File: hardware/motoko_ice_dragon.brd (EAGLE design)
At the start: 91 x 88 mm, 112 parts, among them IC2 LM2937, Q1 8MHz, Q10 20mA/30V, Q11 20mA/30V, Q2 BSS138TOP, Q3 BSS138TOP, Q4 20mA/30V, Q5 20mA/30V, Q6 20mA/30V, Q7 20mA/30V, Q8 20mA/30V, Q9 20mA/30V, U1 MP6540HA, U2 STM32_STM32F722XX, U3 MP6540HA

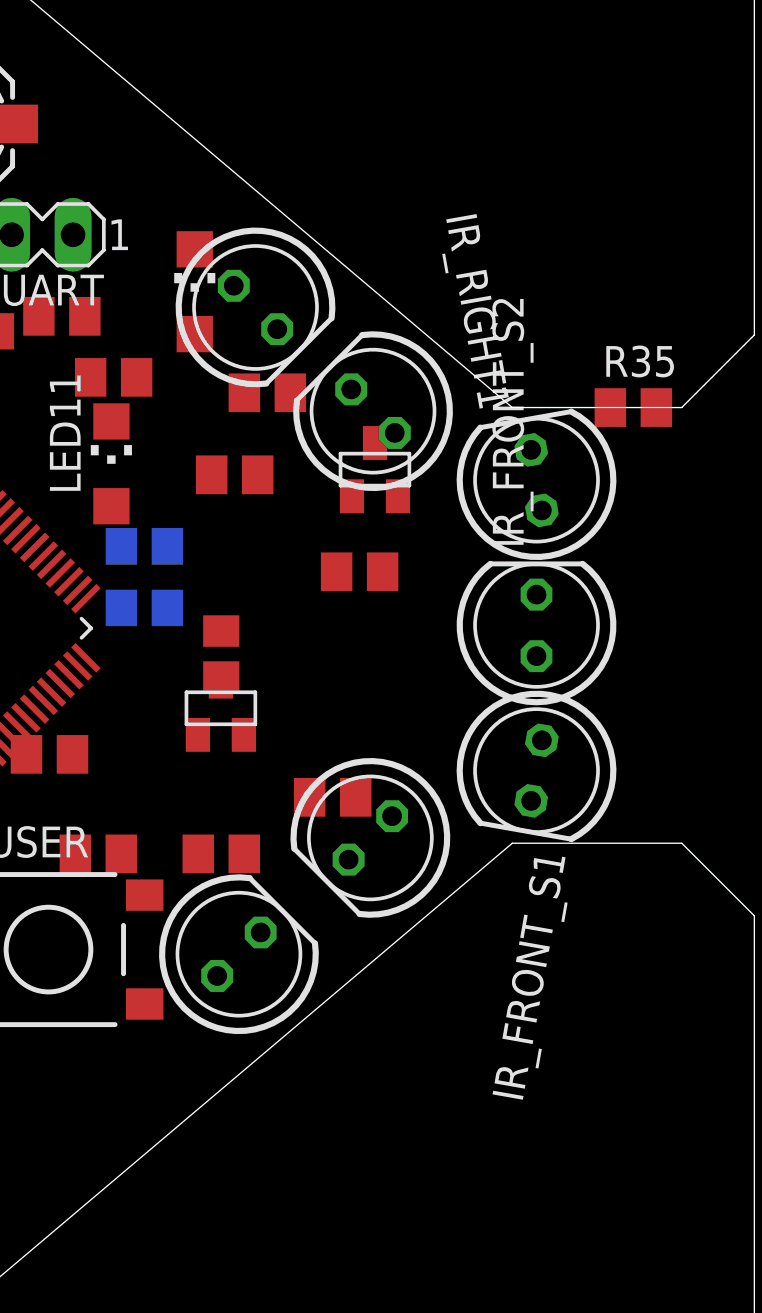
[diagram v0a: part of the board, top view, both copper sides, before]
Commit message: lqr design
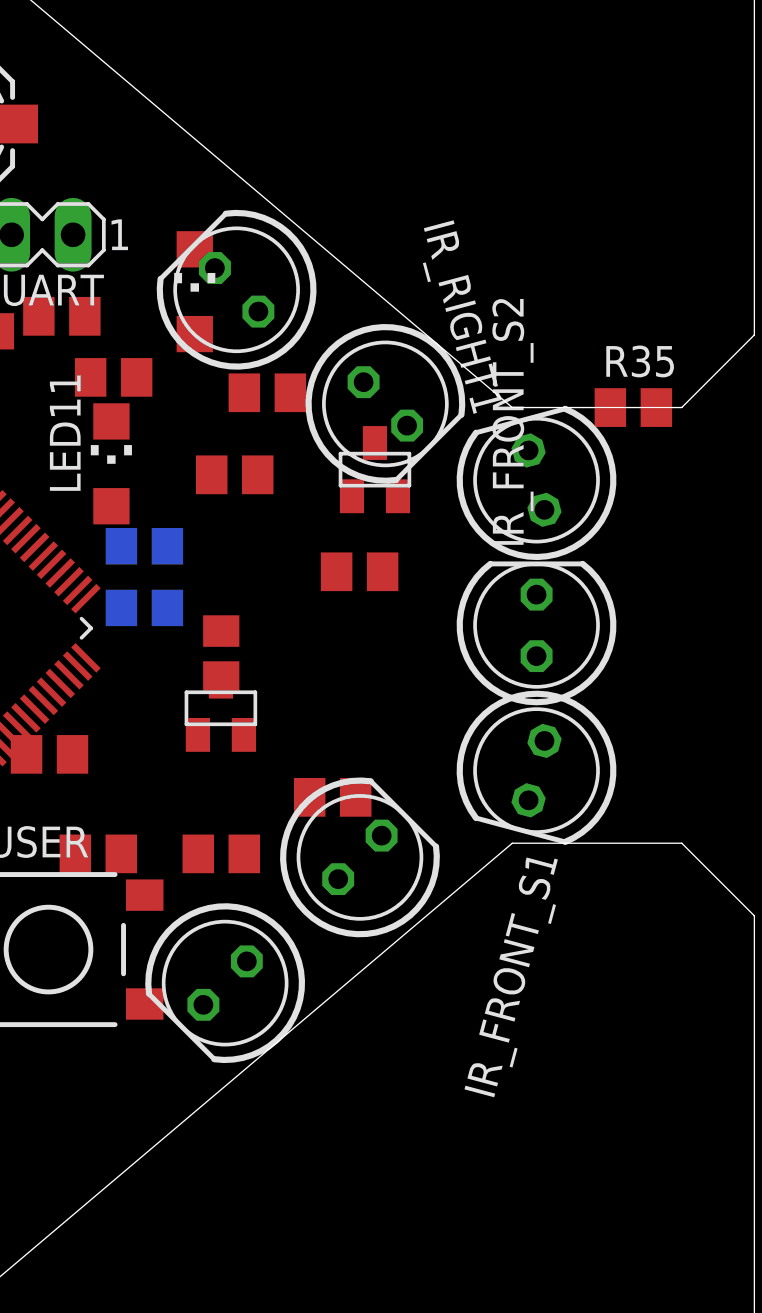
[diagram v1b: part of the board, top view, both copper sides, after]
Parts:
- moved IR_RIGHT 8.49 mm to (54.1, 30.2)
- moved IR_RIGHT_S 6.40 mm to (59.7, 35.4)
- moved IR_LEFT 1.07 mm to (54.6, 58.9), turned to 135 degrees
- moved IR_LEFT_S 0.59 mm to (60.8, 54.1), turned to 315 degrees
- turned IR_FRONT_S1 to 255 degrees
- turned IR_RIGHT1 to 105 degrees
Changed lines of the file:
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@@
 <attribute name="POPULARITY" value="0" x="47.0176" y="-14.2464" size="1.778" layer="28" rot="MR270" display="off"/>
 </element>
-<element name="IR_LEFT" library="my_parts" package="LED5MM" value="" x="55.39" y="58.135" smashed="yes" rot="R315">
-<attribute name="VALUE" x="56.377828125" y="54.59678125" size="1.27" layer="27" ratio="10" rot="R315"/>
-</element>
-<element name="IR_RIGHT" library="my_parts" package="LED5MM" value="" x="60.135" y="36.22" smashed="yes" rot="R225">
-<attribute name="VALUE" x="56.59678125" y="35.232171875" size="1.27" layer="27" ratio="10" rot="R225"/>
-</element>
-<element name="IR_LEFT_S" library="my_parts" package="LED5MM" value="" x="60.245" y="53.85" smashed="yes" rot="R135">
-<attribute name="VALUE" x="59.257171875" y="57.38821875" size="1.27" layer="27" ratio="10" rot="R135"/>
-</element>
-<element name="IR_RIGHT_S" library="my_parts" package="LED5MM" value="" x="54.705" y="31.415" smashed="yes" rot="R45">
-<attribute name="VALUE" x="58.24321875" y="32.402828125" size="1.27" layer="27" ratio="10" rot="R45"/>
+<element name="IR_LEFT" library="my_parts" package="LED5MM" value="" x="54.61" y="58.865" smashed="yes" rot="R135">
+<attribute name="VALUE" x="53.622171875" y="62.40321875" size="1.27" layer="27" ratio="10" rot="R135"/>
+</element>
+<element name="IR_RIGHT" library="my_parts" package="LED5MM" value="" x="54.135" y="30.22" smashed="yes" rot="R225">
+<attribute name="VALUE" x="50.59678125" y="29.232171875" size="1.27" layer="27" ratio="10" rot="R225"/>
+</element>
+<element name="IR_LEFT_S" library="my_parts" package="LED5MM" value="" x="60.755" y="54.15" smashed="yes" rot="R315">
+<attribute name="VALUE" x="61.742828125" y="50.61178125" size="1.27" layer="27" ratio="10" rot="R315"/>
+</element>
+<element name="IR_RIGHT_S" library="my_parts" package="LED5MM" value="" x="59.705" y="35.415" smashed="yes" rot="R45">
+<attribute name="VALUE" x="63.24321875" y="36.402828125" size="1.27" layer="27" ratio="10" rot="R45"/>
 </element>
 <element name="JP1" library="jumper" library_urn="urn:adsk.eagle:library:252" package="JP1" package3d_urn="urn:adsk.eagle:package:15455/1" value="2 CellLi-Pol" x="35.6108" y="67.6148" smashed="yes">
@@
 <element name="U$1" library="my_library" package="BRUSHLESS_GIMBAL_MOTOR_WHEEL" value="BRUSHLESS_GIMBAL_MOTOR_WHEEL" x="15" y="76" smashed="yes" rot="R270"/>
 <element name="U$2" library="my_library" package="BRUSHLESS_GIMBAL_MOTOR_WHEEL" value="BRUSHLESS_GIMBAL_MOTOR_WHEEL" x="15" y="14" smashed="yes" rot="R90"/>
-<element name="IR_FRONT_S1" library="my_parts" package="LED5MM" value="" x="67" y="39" smashed="yes" rot="R260">
-<attribute name="NAME" x="66.973959375" y="35.780615625" size="1.27" layer="25" ratio="10" rot="R260"/>
-<attribute name="VALUE" x="64.66825" y="36.1613875" size="1.27" layer="27" ratio="10" rot="R260"/>
+<element name="IR_FRONT_S1" library="my_parts" package="LED5MM" value="" x="67" y="39" smashed="yes" rot="R255">
+<attribute name="NAME" x="66.69346875" y="35.7951375" size="1.27" layer="25" ratio="10" rot="R255"/>
+<attribute name="VALUE" x="64.42971875" y="36.375415625" size="1.27" layer="27" ratio="10" rot="R255"/>
 </element>
 <element name="R35" library="resistor" library_urn="urn:adsk.eagle:library:348" package="M0805" package3d_urn="urn:adsk.eagle:package:26079/1" value="4k7" x="71" y="54" smashed="yes">
@@
 <attribute name="VALUE" x="68.8034" y="48.2004" size="1.27" layer="27" ratio="10" rot="R90"/>
 </element>
-<element name="IR_RIGHT1" library="my_parts" package="LED5MM" value="" x="67" y="51" smashed="yes" rot="R100">
-<attribute name="NAME" x="65.923371875" y="54.034140625" size="1.27" layer="25" ratio="10" rot="R100"/>
-<attribute name="VALUE" x="68.220259375" y="54.464934375" size="1.27" layer="27" ratio="10" rot="R100"/>
+<element name="IR_RIGHT1" library="my_parts" package="LED5MM" value="" x="67" y="51" smashed="yes" rot="R105">
+<attribute name="NAME" x="65.663028125" y="53.928759375" size="1.27" layer="25" ratio="10" rot="R105"/>
+<attribute name="VALUE" x="67.913628125" y="54.5581" size="1.27" layer="27" ratio="10" rot="R105"/>
 </element>
 </elements>
@@
 <wire x1="85.05" y1="20" x2="85.05" y2="30" width="0" layer="19" extent="16-16"/>
 <wire x1="85.05" y1="10" x2="85.05" y2="20" width="0" layer="19" extent="16-16"/>
-<wire x1="67.22053125" y1="40.250703125" x2="85.05" y2="40" width="0" layer="19" extent="16-16"/>
-<wire x1="67" y1="43.73" x2="67.22053125" y2="40.250703125" width="0" layer="19" extent="1-1"/>
+<wire x1="67" y1="43.73" x2="85.05" y2="40" width="0" layer="19" extent="16-16"/>
+<wire x1="67.3287" y1="40.226725" x2="67" y2="43.73" width="0" layer="19" extent="1-1"/>
 <wire x1="61.275" y1="50.335" x2="67" y2="43.73" width="0" layer="19" extent="1-1"/>
-<wire x1="61.143025" y1="52.951971875" x2="61.275" y2="50.335" width="0" layer="19" extent="1-1"/>
-<wire x1="56.83" y1="54.61" x2="61.143025" y2="52.951971875" width="0" layer="19" extent="1-1"/>
+<wire x1="59.856971875" y1="55.048025" x2="61.275" y2="50.335" width="0" layer="19" extent="1-1"/>
+<wire x1="56.83" y1="54.61" x2="59.856971875" y2="55.048025" width="0" layer="19" extent="1-1"/>
 <wire x1="52.88" y1="60.535" x2="56.83" y2="54.61" width="0" layer="19" extent="1-1"/>
 <wire x1="49.435" y1="53.425" x2="56.83" y2="54.61" width="0" layer="19" extent="1-1"/>
@@
 <wire x1="31.6992" y1="73.6092" x2="35.4524" y2="72.3636" width="0" layer="19" extent="1-1"/>
 <wire x1="50.8126" y1="33.856" x2="43.9142" y2="30.6588" width="0" layer="19" extent="1-1"/>
-<wire x1="53.806971875" y1="30.516971875" x2="50.8126" y2="33.856" width="0" layer="19" extent="1-1"/>
+<wire x1="58.806971875" y1="34.516971875" x2="50.8126" y2="33.856" width="0" layer="19" extent="1-1"/>
 <wire x1="38.415" y1="22.225" x2="39.69" y2="30.48" width="0" layer="19" extent="1-16"/>
 <wire x1="32.004" y1="16.002" x2="38.415" y2="22.225" width="0" layer="19" extent="1-1"/>
@@
 <contactref element="IR_FRONT_S2" pad="K"/>
 <wire x1="67" y1="46.27" x2="70.05" y2="54" width="0" layer="19" extent="1-1"/>
-<wire x1="66.779465625" y1="37.74929375" x2="67" y2="46.27" width="0" layer="19" extent="1-1"/>
-<wire x1="53.025" y1="35.56" x2="66.779465625" y2="37.74929375" width="0" layer="19" extent="1-1"/>
+<wire x1="66.671296875" y1="37.773271875" x2="67" y2="46.27" width="0" layer="19" extent="1-1"/>
+<wire x1="53.025" y1="35.56" x2="66.671296875" y2="37.773271875" width="0" layer="19" extent="1-1"/>
 <wire x1="46.263534375" y1="48.222453125" x2="53.025" y2="35.56" width="0" layer="19" extent="1-1"/>
 </signal>
@@
 <contactref element="R29" pad="1"/>
 <contactref element="IR_RIGHT1" pad="A"/>
-<wire x1="60.64" y1="47.215" x2="67.22053125" y2="49.74929375" width="0" layer="19" extent="1-1"/>
+<wire x1="60.64" y1="47.215" x2="67.3287" y2="49.773271875" width="0" layer="19" extent="1-1"/>
 </signal>
 <signal name="IR_LED_FRONT">
@@
 <contactref element="IR_LEFT" pad="K"/>
 <contactref element="IR_RIGHT1" pad="K"/>
-<wire x1="56.288025" y1="57.236971875" x2="66.779465625" y2="52.250703125" width="0" layer="19" extent="1-1"/>
-<wire x1="53.96" y1="42.675" x2="56.288025" y2="57.236971875" width="0" layer="19" extent="1-1"/>
-<wire x1="59.236971875" y1="35.321971875" x2="53.96" y2="42.675" width="0" layer="19" extent="1-1"/>
+<wire x1="53.711971875" y1="59.763025" x2="66.671296875" y2="52.226725" width="0" layer="19" extent="1-1"/>
+<wire x1="53.96" y1="42.675" x2="53.711971875" y2="59.763025" width="0" layer="19" extent="1-1"/>
+<wire x1="53.236971875" y1="29.321971875" x2="53.96" y2="42.675" width="0" layer="19" extent="1-1"/>
 </signal>
 <signal name="IR_LED_CONTROLL">
@@
 <contactref element="U2" pad="33"/>
 <wire x1="47.945" y1="35.56" x2="45.904325" y2="48.5816625" width="0" layer="19" extent="1-1"/>
-<wire x1="55.603025" y1="32.313025" x2="47.945" y2="35.56" width="0" layer="19" extent="1-1"/>
+<wire x1="60.603025" y1="36.313025" x2="47.945" y2="35.56" width="0" layer="19" extent="1-1"/>
 </signal>
 <signal name="ADC10">
@@
 <contactref element="IR_LEFT_S" pad="K"/>
 <contactref element="U2" pad="34"/>
-<wire x1="45.563075" y1="48.9229125" x2="59.346971875" y2="54.748025" width="0" layer="19" extent="1-1"/>
+<wire x1="45.563075" y1="48.9229125" x2="61.653025" y2="53.251971875" width="0" layer="19" extent="1-1"/>
 <wire x1="45.93" y1="39.67" x2="45.563075" y2="48.9229125" width="0" layer="19" extent="1-1"/>
 </signal>
@@
 <contactref element="R31" pad="1"/>
 <contactref element="IR_RIGHT" pad="A"/>
-<wire x1="57.63" y1="37.895" x2="61.033025" y2="37.118025" width="0" layer="19" extent="1-1"/>
+<wire x1="57.63" y1="37.895" x2="55.033025" y2="31.118025" width="0" layer="19" extent="1-1"/>
 </signal>
 <signal name="N$13">
 <contactref element="R33" pad="1"/>
 <contactref element="IR_LEFT" pad="A"/>
-<wire x1="46.44" y1="57.77" x2="54.491971875" y2="59.033025" width="0" layer="19" extent="1-1"/>
+<wire x1="46.44" y1="57.77" x2="55.508025" y2="57.966971875" width="0" layer="19" extent="1-1"/>
 </signal>
 <signal name="LINE_LED">
